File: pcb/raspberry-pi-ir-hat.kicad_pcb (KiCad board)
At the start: 2 copper layers, 42.7 x 84.5 mm, 22 parts, among them J1 IO, J2 TX, J3 RX, J4 RX_JMP, J5 TX_JMP, J6 RW_JMP, J7 Raspberry_Pi_2_3, Q1 Q_NMOS_GSD

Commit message: update pcb
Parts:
- removed D2: RX, LED_SMD:LED_0805_2012Metric
- removed R2: 10K, Resistor_SMD:R_0805_2012Metric
- removed R4: 1K, Resistor_SMD:R_0805_2012Metric
- R1: value 222 -> 100
- R3, R5, R6: value 1K -> 100
- moved D3 25.7 mm to (128.3, 81.0), turned to 270 degrees
- moved R5 17.7 mm to (128.3, 85.2), turned to 90 degrees
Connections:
- net /MISC renamed /RXLED
- J4 pad 2: GND -> /RX
- J4 pad 4: VCC -> GND
- J4 pad 6: /RX -> VCC
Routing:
- net Net-(D2-Pad2): track 57.0 -> 0.00 mm, vias 2 -> 0
- net /5V: track 49.8 -> 33.2 mm
- net VCC: track 114.6 -> 106.0 mm, vias 4 -> 2
- net GND: track 3.27 -> 9.72 mm
- net /RXLED: track 22.6 -> 25.5 mm, vias 0 -> 4
- net /RX: track 66.8 -> 69.0 mm
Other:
- board text added: "+"
- board text added: "-"
- board text added: "2020-10-21"
- board text removed: "2020-10-01"
- board text removed: "MISC"
- board text removed: "RNG"
- board text removed: "SLV"
- board text removed: "TIP"

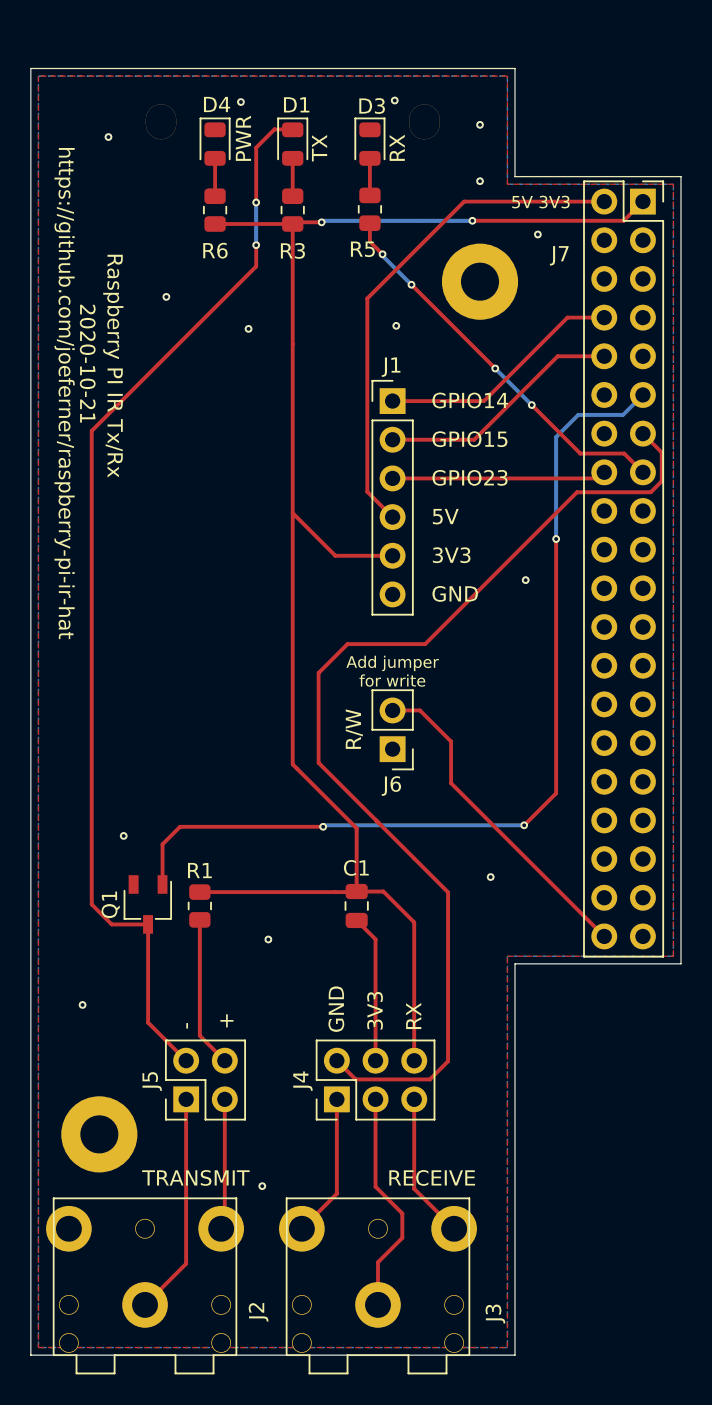
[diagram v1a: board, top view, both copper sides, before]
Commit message: add stm32 to pcb
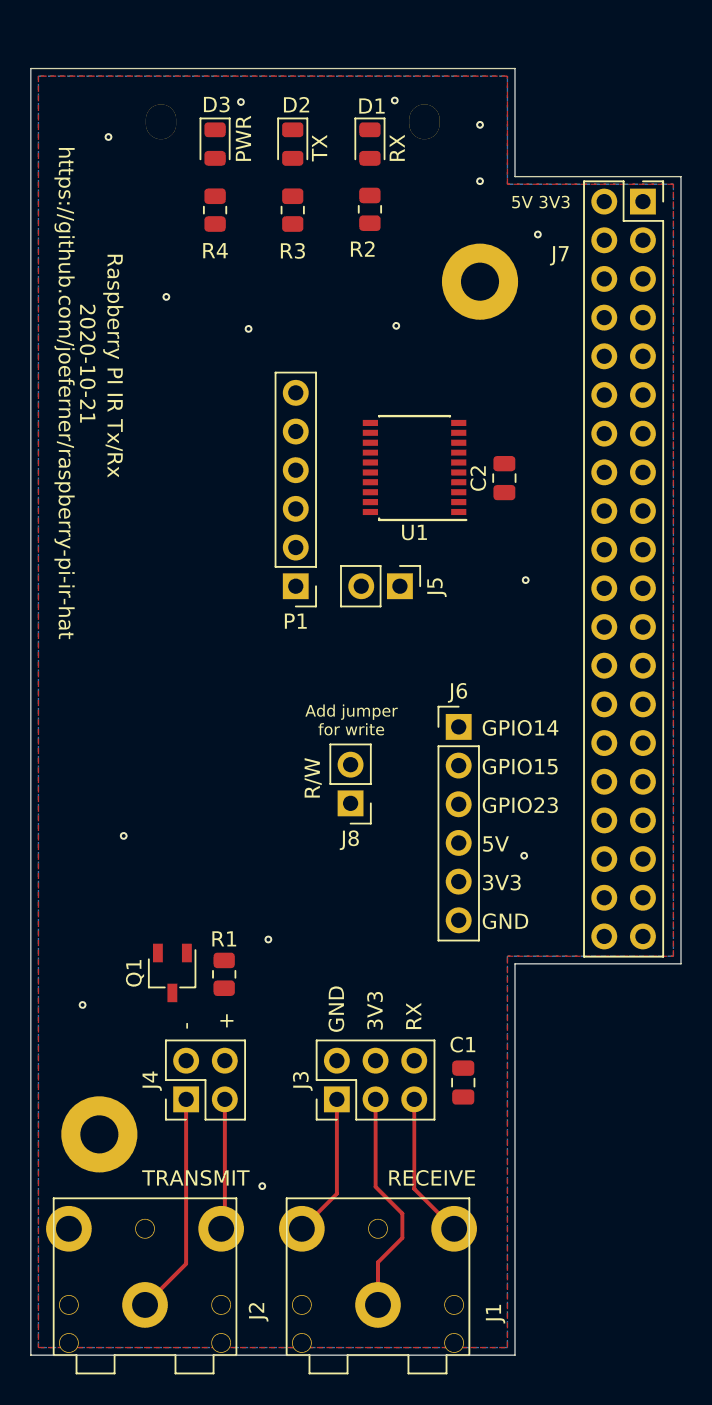
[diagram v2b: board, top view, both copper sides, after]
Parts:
- removed the J1 at (129.8, 97.8)
- added C2: 0.1uF, Capacitor_SMD:C_0805_2012Metric, F.Cu at (137.1, 102.9)
- added J5: SWD_VCC, Connector_PinHeader_2.54mm:PinHeader_1x02_P2.54mm_Vertical, F.Cu at (130.2, 110.0)
- added J8: RW_JMP, Connector_PinHeader_2.54mm:PinHeader_1x02_P2.54mm_Vertical, F.Cu at (127.0, 124.3)
- added P1: ST-SWD, Connector_PinHeader_2.54mm:PinHeader_1x06_P2.54mm_Vertical, F.Cu at (123.4, 110.0)
- added U1: STM32G030Fx_TSSOP20, Housings_SSOP:SSOP-20_4.4x6.5mm_Pitch0.65mm, F.Cu at (131.2, 102.2)
- D3: renamed from D4; value RX -> POWER
- J6: value RW_JMP -> IO; footprint Connector_PinHeader_2.54mm:PinHeader_1x02_P2.54mm_Vertical -> Connector_PinHeader_2.54mm:PinHeader_1x06_P2.54mm_Vertical
- moved C1 13.5 mm to (134.4, 142.6)
- moved Q1 4.78 mm to (115.3, 135.4)
- moved R1 4.76 mm to (118.7, 135.5)
- moved J6 4.58 mm to (134.1, 119.2), turned to 0 degrees
- renumbered D3 to D1, D1 to D2, J3 to J1, J4 to J3, J5 to J4, R5 to R2, R6 to R4
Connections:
- J3 pad 2: /RX -> /IR_RX
- J6 pad 1: GND -> /IO1
- J6 pad 2: /RW -> /IO2
- J7 pad 10: /IO2 -> /RPI_USART_RX
- J7 pad 11: /TX -> /MCU_RESET
- J7 pad 12: Net-(J7-Pad12) -> /MCU_BOOT0
- J7 pad 13: /RX -> Net-(J7-Pad13)
- J7 pad 15: /RXLED -> /IO1
- J7 pad 16: /IO3 -> /IO2
- J7 pad 18: Net-(J7-Pad18) -> /IO3
- J7 pad 8: /IO1 -> /RPI_USART_TX
- Q1 pad 1: /TX -> /IR_TX
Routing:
- net VCC: track 106.0 -> 0.00 mm, vias 2 -> 0
- net Net-(D2-Pad1): track 71.3 -> 0.00 mm, vias 2 -> 0
- net /RX: track 69.0 -> 0.00 mm
- net /TX: track 60.1 -> 0.00 mm, vias 3 -> 0
- net /5V: track 33.2 -> 0.00 mm
- net /RXLED: track 25.5 -> 0.00 mm, vias 4 -> 0
- net /RW: track 21.7 -> 0.00 mm
- net /IO1: track 16.2 -> 0.00 mm
- net /IO2: track 16.2 -> 0.00 mm
- net /IO3: track 14.1 -> 0.00 mm
- net Net-(J4-Pad4): track 9.93 -> 0.00 mm
- net GND: track 9.72 -> 0.00 mm
- net Net-(D2-Pad2): track 2.51 -> 0.00 mm
- net Net-(D3-Pad2): track 2.49 -> 0.00 mm
- net Net-(D1-Pad2): track 2.43 -> 0.00 mm

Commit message: update schematic and pcb with mcu
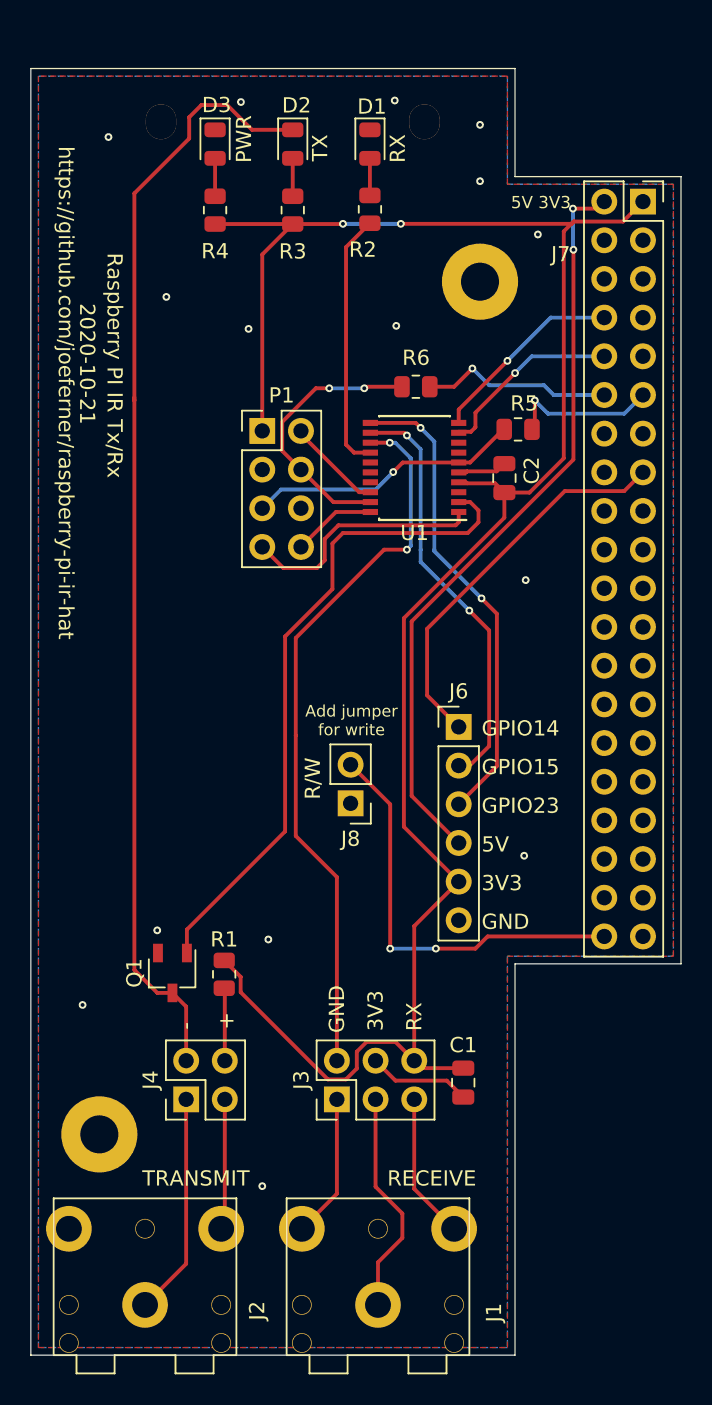
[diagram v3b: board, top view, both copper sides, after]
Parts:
- removed J5: SWD_VCC, Connector_PinHeader_2.54mm:PinHeader_1x02_P2.54mm_Vertical
- added R5: 10K, Resistor_SMD:R_0805_2012Metric, F.Cu at (138.0, 99.7)
- added R6: 10K, Resistor_SMD:R_0805_2012Metric, F.Cu at (131.3, 96.9)
- J1, J2: footprint modules:CUIDEVICES-SJ1-3523NG -> kicad-library:CUIDEVICES-SJ1-3523NG
- P1: value ST-SWD -> ST_PROGRAM_DEBUG; footprint Connector_PinHeader_2.54mm:PinHeader_1x06_P2.54mm_Vertical -> Connector_PinHeader_2.54mm:PinHeader_2x04_P2.54mm_Vertical
- REF**: footprint modules:BIVAR-RLP3-200-500 -> kicad-library:BIVAR-RLP3-200-500
- moved P1 10.4 mm to (121.2, 99.8), turned to 0 degrees
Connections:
- J7 pad 11: /MCU_RESET -> Net-(J7-Pad11)
- J7 pad 12: /MCU_BOOT0 -> Net-(J7-Pad12)
- J7 pad 16: /IO2 -> Net-(J7-Pad16)
- J7 pad 18: /IO3 -> Net-(J7-Pad18)
- P1 pad 1: Net-(J5-Pad2) -> VCC
- P1 pad 2: /MCU_BOOT0 -> /SWDIO
- P1 pad 4: /SWDIO -> /MCU_BOOT0
- U1 pad 1: Net-(U1-Pad1) -> /DEBUG_RX
- U1 pad 11: Net-(U1-Pad11) -> /IO3
- U1 pad 12: Net-(U1-Pad12) -> /IO2
- U1 pad 20: Net-(U1-Pad20) -> /DEBUG_TX
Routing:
- net VCC: track 0.00 -> 131.7 mm, vias 0 -> 2
- net Net-(D2-Pad1): track 0.00 -> 73.4 mm
- net /5V: track 0.00 -> 49.6 mm, vias 0 -> 2
- net /IR_RX: track 0.00 -> 47.8 mm, vias 0 -> 2
- net /IR_TX: track 0.00 -> 43.3 mm
- net /IO3: track 0.00 -> 31.3 mm, vias 0 -> 2
- net /IO2: track 0.00 -> 27.6 mm, vias 0 -> 2
- net /RW: track 0.00 -> 27.5 mm, vias 0 -> 2
- net /IO1: track 0.00 -> 25.7 mm
- net /MCU_RESET: track 0.00 -> 18.0 mm, vias 0 -> 1
- net /MCU_BOOT0: track 0.00 -> 17.9 mm, vias 0 -> 2
- net /RXLED: track 0.00 -> 17.0 mm
- net /DEBUG_RX: track 0.00 -> 16.2 mm
- net /RPI_USART_TX: track 0.00 -> 12.9 mm, vias 0 -> 1
- net Net-(J7-Pad12): track 0.00 -> 12.7 mm, vias 0 -> 1
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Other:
- net class Default: clearance 0.254 -> 0.1524
- rule trace_clearance: 0.254 -> 0.1524

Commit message: update pcbs
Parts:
- P1: footprint Connector_PinHeader_2.54mm:PinHeader_2x04_P2.54mm_Vertical -> kicad-library:PinHeader_2x04_P2.54mm_Vertical_Shrouded
- moved P1 3.20 mm to (118.0, 99.8)
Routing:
- net /MCU_BOOT0: track 17.9 -> 24.6 mm
- net /MCU_RESET: track 18.0 -> 21.2 mm
- net /DEBUG_TX: track 5.51 -> 8.71 mm
- net /SWDIO: track 6.34 -> 9.43 mm
- net /DEBUG_RX: track 16.2 -> 18.6 mm
- net VCC: track 131.7 -> 133.0 mm
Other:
- board text added: "2020-10-30"
- board text added: "CLK"
- board text added: "IO"
- board text added: "RST"
- board text added: "SWD"
- board text added: "VCC"
- board text removed: "2020-10-21"
